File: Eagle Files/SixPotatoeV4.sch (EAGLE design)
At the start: 27 parts, among them J3 IMU, J4 ON/OFF, J5 GND, J6 3.3v

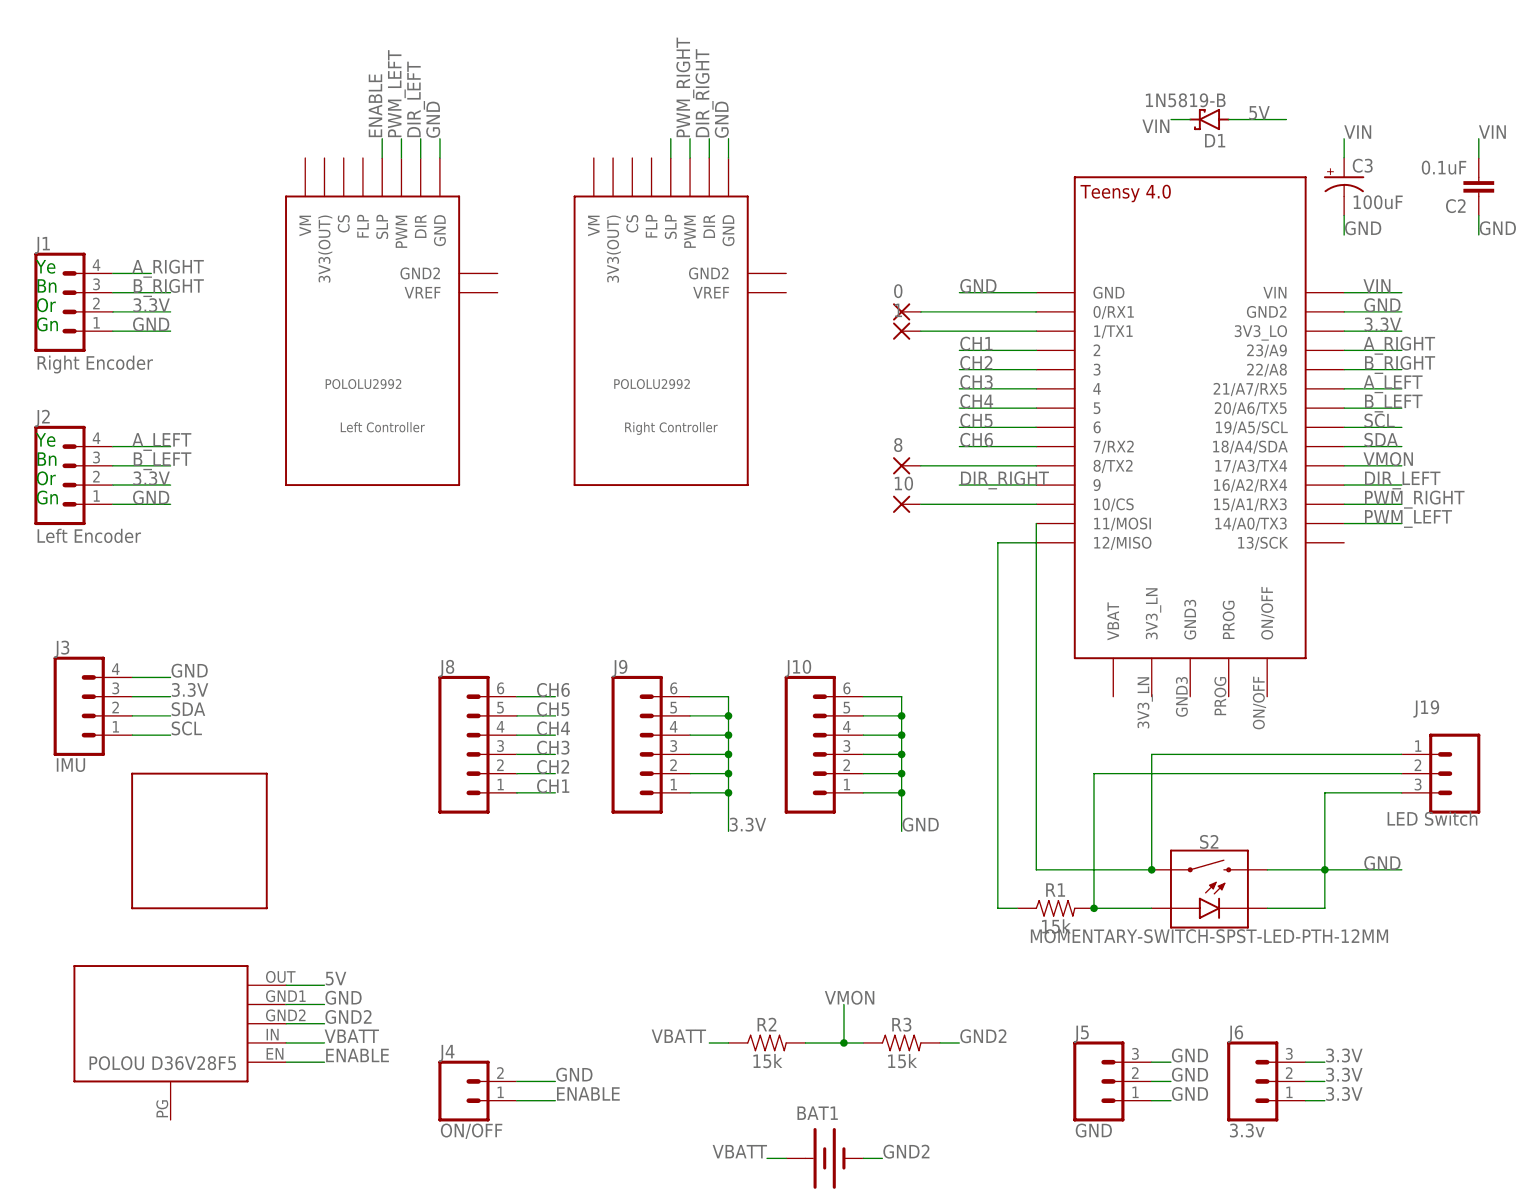
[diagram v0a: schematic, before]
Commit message: Video completed
Also, excess code removed, first routes checked out.
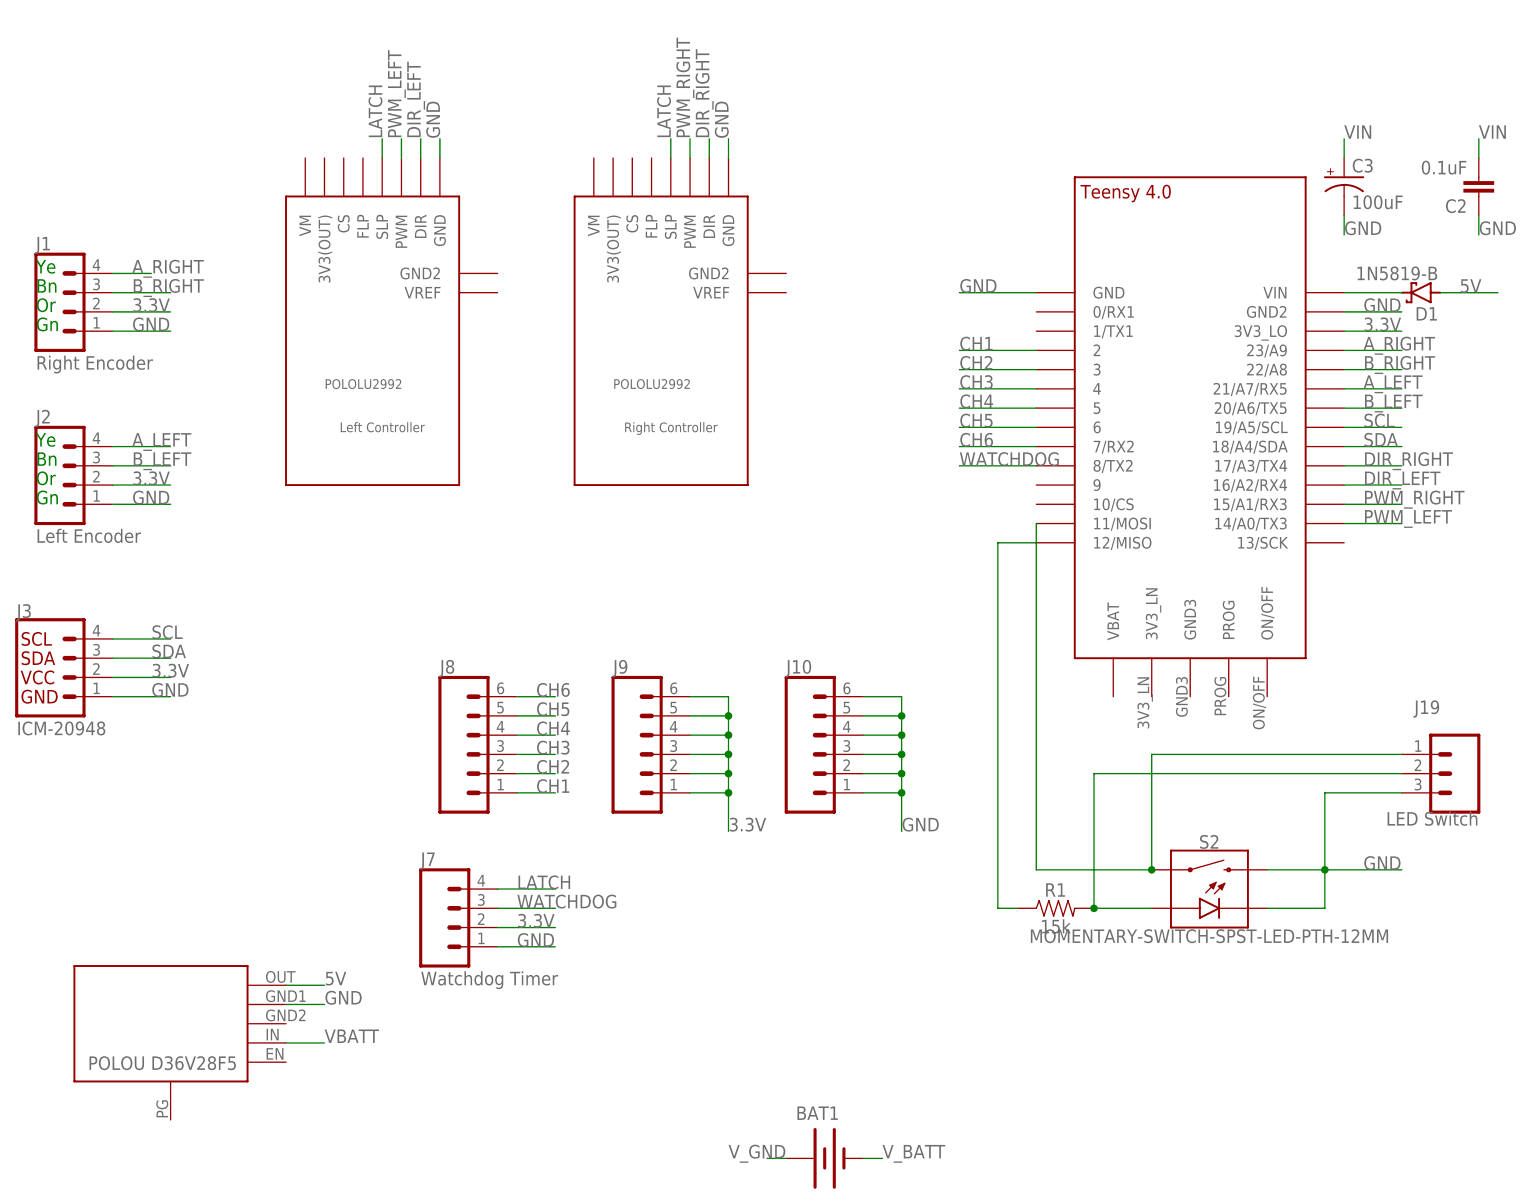
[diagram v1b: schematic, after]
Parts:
- removed 0, 1, 10, 8: (no value), wirepad:2,15/1,0
- removed J4: ON/OFF, SparkFun-Connectors:CONN_02
- removed J5: GND, SparkFun-Connectors:CONN_03
- removed J6: 3.3v, SparkFun-Connectors:CONN_03
- removed R2, R3: 15k, SparkFun-Resistors:15KOHM-HORIZ-1/4W-5%
- removed U$5: SEN15335_NO_PTH, TimEagleLibrary:SEN15335_NO_PTH
- added J7: (no value), SparkFun-Connectors:CONN_04
- J3: value IMU -> (none); device SparkFun-Connectors:CONN_04 -> SparkFun-Connectors:I2C_STANDARD; ID (none) -> ICM-20948
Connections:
- removed net ENABLE: J4.1, U$2.SLP, U$3.SLP, U$4.EN
- removed net GND2: BAT1.-, R3.2, U$4.GND2
- removed net N$5: 1.P, U$1.1/TX1
- removed net N$6: 10.P, U$1.10/CS
- removed net N$7: 8.P, U$1.8/TX2
- removed net VMON: R2.2, R3.1, U$1.17/A3/TX4
- new net LATCH: J7.4, U$2.SLP, U$3.SLP
- new net V_BATT: BAT1.-
- new net V_GND: BAT1.+
- new net WATCHDOG: J7.3, U$1.8/TX2
- net 3.3V: now also J3.2, J7.2; no longer J3.3, J6.1, J6.2, J6.3
- net DIR_RIGHT: now also U$1.17/A3/TX4; no longer U$1.9
- net GND: now also J3.1, J7.1; no longer J3.4, J4.2, J5.1, J5.2, J5.3
- net N$1: now also D1.C, U$1.VIN; no longer 0.P, U$1.0/RX1
- net SCL: now also J3.4; no longer J3.1
- net SDA: now also J3.3; no longer J3.2
- net VBATT: no longer BAT1.+, R2.1
- net VIN: no longer D1.C, U$1.VIN
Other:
- moved on the sheet: D1
